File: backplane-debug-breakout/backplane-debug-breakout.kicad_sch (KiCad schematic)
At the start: 9 parts, among them J1 Conn_02x08_Odd_Even, J2 Conn_01x04, J3 Conn_01x01_Socket, J4 Conn_01x01_Socket, J5 Conn_01x04, SW1 SW_Push

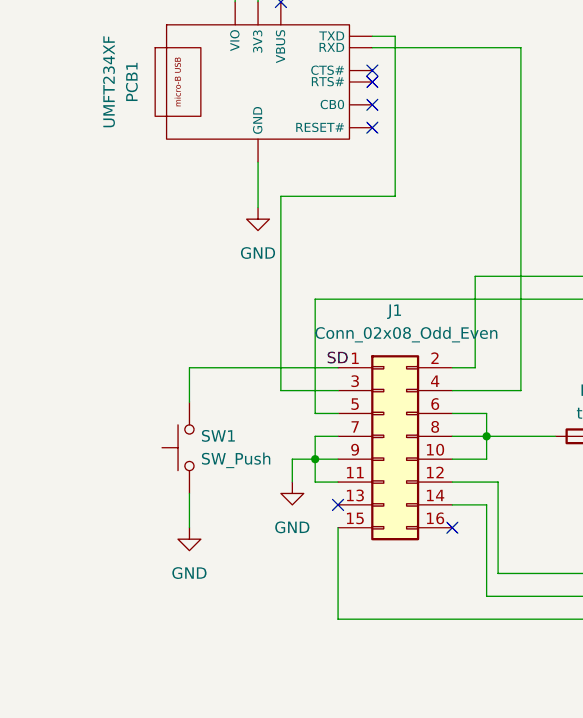
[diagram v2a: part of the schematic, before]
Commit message: added slide switch in parallel with push button
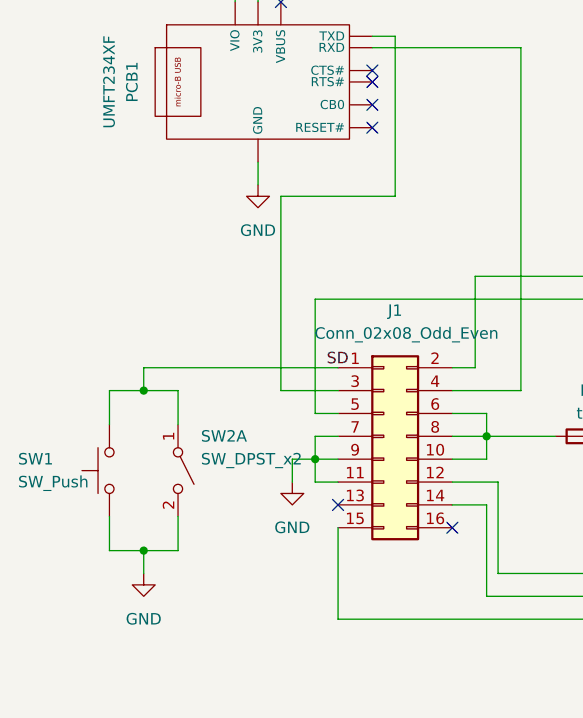
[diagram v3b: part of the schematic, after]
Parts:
- added SW2: SW_DPST_x2, symbol Switch:SW_DPST_x2
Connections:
- net GND: now also SW2.2 (B)
- net SD: now also SW2.1 (A)
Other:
- moved on the sheet: SW1
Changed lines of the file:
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@@
   (junction (at 101.6 82.55) (diameter 0) (color 0 0 0 0)
   )
+  (junction (at 82.55 74.93) (diameter 0) (color 0 0 0 0)
+  )
   (junction (at 120.65 80.01) (diameter 0) (color 0 0 0 0)
+  )
+  (junction (at 82.55 92.71) (diameter 0) (color 0 0 0 0)
   )
   (no_connect (at 148.59 67.31))
@@
     (stroke (width 0) (type default))
   )
+  (wire (pts (xy 78.74 74.93) (xy 82.55 74.93))
+    (stroke (width 0) (type default))
+  )
   (wire (pts (xy 101.6 82.55) (xy 101.6 85.09))
     (stroke (width 0) (type default))
   )
+  (wire (pts (xy 78.74 92.71) (xy 82.55 92.71))
+    (stroke (width 0) (type default))
+  )
   (wire (pts (xy 101.6 77.47) (xy 101.6 64.77))
     (stroke (width 0) (type default))
   )
+  (wire (pts (xy 78.74 78.74) (xy 78.74 74.93))
+    (stroke (width 0) (type default))
+  )
   (wire (pts (xy 116.84 82.55) (xy 120.65 82.55))
     (stroke (width 0) (type default))
@@
     (stroke (width 0) (type default))
   )
+  (wire (pts (xy 82.55 92.71) (xy 86.36 92.71))
+    (stroke (width 0) (type default))
+  )
   (wire (pts (xy 124.46 36.83) (xy 107.95 36.83))
     (stroke (width 0) (type default))
@@
     (stroke (width 0) (type default))
   )
-  (wire (pts (xy 87.63 72.39) (xy 104.14 72.39))
+  (wire (pts (xy 82.55 72.39) (xy 104.14 72.39))
     (stroke (width 0) (type default))
   )
@@
     (stroke (width 0) (type default))
   )
-  (wire (pts (xy 87.63 76.2) (xy 87.63 72.39))
-    (stroke (width 0) (type default))
-  )
   (wire (pts (xy 116.84 77.47) (xy 120.65 77.47))
     (stroke (width 0) (type default))
@@
     (stroke (width 0) (type default))
   )
-  (wire (pts (xy 87.63 86.36) (xy 87.63 90.17))
+  (wire (pts (xy 78.74 88.9) (xy 78.74 92.71))
     (stroke (width 0) (type default))
   )
@@
     (stroke (width 0) (type default))
   )
+  (wire (pts (xy 86.36 88.9) (xy 86.36 92.71))
+    (stroke (width 0) (type default))
+  )
+  (wire (pts (xy 82.55 92.71) (xy 82.55 95.25))
+    (stroke (width 0) (type default))
+  )
   (wire (pts (xy 101.6 80.01) (xy 101.6 82.55))
     (stroke (width 0) (type default))
@@
     (stroke (width 0) (type default))
   )
+  (wire (pts (xy 82.55 72.39) (xy 82.55 74.93))
+    (stroke (width 0) (type default))
+  )
   (wire (pts (xy 99.06 82.55) (xy 101.6 82.55))
     (stroke (width 0) (type default))
   )
+  (wire (pts (xy 86.36 74.93) (xy 86.36 78.74))
+    (stroke (width 0) (type default))
+  )
   (wire (pts (xy 154.94 83.82) (xy 154.94 86.36))
     (stroke (width 0) (type default))
   )
-  (wire (pts (xy 95.25 49.53) (xy 95.25 54.61))
+  (wire (pts (xy 82.55 74.93) (xy 86.36 74.93))
+    (stroke (width 0) (type default))
+  )
+  (wire (pts (xy 95.25 49.53) (xy 95.25 52.07))
     (stroke (width 0) (type default))
   )
@@
     )
   )
-  (symbol (lib_id "power:GND") (at 95.25 54.61 0) (unit 1)
+  (symbol (lib_id "power:GND") (at 95.25 52.07 0) (unit 1)
     (in_bom yes) (on_board yes) (dnp no) (fields_autoplaced)
-    (property "Reference" "#PWR06" (at 95.25 60.96 0)
-      (effects (font (size 1.27 1.27)) hide)
-    )
-    (property "Value" "GND" (at 95.25 59.69 0)
-      (effects (font (size 1.27 1.27)))
-    )
-    (property "Footprint" "" (at 95.25 54.61 0)
-      (effects (font (size 1.27 1.27)) hide)
-    )
-    (property "Datasheet" "" (at 95.25 54.61 0)
+    (property "Reference" "#PWR06" (at 95.25 58.42 0)
+      (effects (font (size 1.27 1.27)) hide)
+    )
+    (property "Value" "GND" (at 95.25 57.15 0)
+      (effects (font (size 1.27 1.27)))
+    )
+    (property "Footprint" "" (at 95.25 52.07 0)
+      (effects (font (size 1.27 1.27)) hide)
+    )
+    (property "Datasheet" "" (at 95.25 52.07 0)
       (effects (font (size 1.27 1.27)) hide)
     )
@@
     )
   )
-  (symbol (lib_id "power:GND") (at 87.63 90.17 0) (unit 1)
+  (symbol (lib_id "power:GND") (at 82.55 95.25 0) (unit 1)
     (in_bom yes) (on_board yes) (dnp no) (fields_autoplaced)
-    (property "Reference" "#PWR01" (at 87.63 96.52 0)
-      (effects (font (size 1.27 1.27)) hide)
-    )
-    (property "Value" "GND" (at 87.63 95.25 0)
-      (effects (font (size 1.27 1.27)))
-    )
-    (property "Footprint" "" (at 87.63 90.17 0)
-      (effects (font (size 1.27 1.27)) hide)
-    )
-    (property "Datasheet" "" (at 87.63 90.17 0)
+    (property "Reference" "#PWR01" (at 82.55 101.6 0)
+      (effects (font (size 1.27 1.27)) hide)
+    )
+    (property "Value" "GND" (at 82.55 100.33 0)
+      (effects (font (size 1.27 1.27)))
+    )
+    (property "Footprint" "" (at 82.55 95.25 0)
+      (effects (font (size 1.27 1.27)) hide)
+    )
+    (property "Datasheet" "" (at 82.55 95.25 0)
       (effects (font (size 1.27 1.27)) hide)
     )
@@
     )
   )
+  (symbol (lib_id "Switch:SW_DPST_x2") (at 86.36 83.82 270) (unit 1)
+    (in_bom yes) (on_board yes) (dnp no)
+    (property "Reference" "SW2" (at 88.9 80.01 90)
+      (effects (font (size 1.27 1.27)) (justify left))
+    )
+    (property "Value" "SW_DPST_x2" (at 88.9 82.55 90)
+      (effects (font (size 1.27 1.27)) (justify left))
+    )
+    (property "Footprint" "" (at 86.36 83.82 0)
+      (effects (font (size 1.27 1.27)) hide)
+    )
+    (property "Datasheet" "~" (at 86.36 83.82 0)
+      (effects (font (size 1.27 1.27)) hide)
+    )
+    (pin "4")
+    (pin "3")
+    (pin "2")
+    (pin "1")
+    (instances
+      (project "backplane-debug-breakout"
+        (path "/3c6f9748-3b52-445b-9cee-a3f7ec926272"
+          (reference "SW2") (unit 1)
+        )
+      )
+    )
+  )
   (symbol (lib_id "Connector_Generic:Conn_01x04") (at 153.67 62.23 0) (unit 1)
     (in_bom yes) (on_board yes) (dnp no)
@@
     )
   )
-  (symbol (lib_id "Switch:SW_Push") (at 87.63 81.28 90) (unit 1)
-    (in_bom yes) (on_board yes) (dnp no) (fields_autoplaced)
-    (property "Reference" "SW1" (at 88.9 80.01 90)
+  (symbol (lib_id "Switch:SW_Push") (at 78.74 83.82 90) (unit 1)
+    (in_bom yes) (on_board yes) (dnp no)
+    (property "Reference" "SW1" (at 68.58 82.55 90)
       (effects (font (size 1.27 1.27)) (justify right))
     )
-    (property "Value" "SW_Push" (at 88.9 82.55 90)
+    (property "Value" "SW_Push" (at 68.58 85.09 90)
       (effects (font (size 1.27 1.27)) (justify right))
     )
-    (property "Footprint" "" (at 82.55 81.28 0)
-      (effects (font (size 1.27 1.27)) hide)
-    )
-    (property "Datasheet" "~" (at 82.55 81.28 0)
-      (effects (font (size 1.27 1.27)) hide)
-    )
+    (property "Footprint" "" (at 73.66 83.82 0)
+      (effects (font (size 1.27 1.27)) hide)
+    )
+    (property "Datasheet" "~" (at 73.66 83.82 0)
+      (effects (font (size 1.27 1.27)) hide)
+    )

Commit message: finished schematic.
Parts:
- removed F1: tbd, symbol Device:Fuse
- added F2: Fuse_Small, oresat-passives:Littelfuse 155900DR, symbol Device:Fuse_Small
- D1: footprint Diode_THT:D_DO-41_SOD81_P10.16mm_Horizontal -> oresat-diodes:Diode TSM MURS315SH
- J1: footprint (none) -> Connector_PinHeader_2.54mm:PinHeader_2x08_P2.54mm_Vertical
- J2: footprint (none) -> Connector_PinHeader_2.54mm:PinHeader_1x04_P2.54mm_Vertical
- J3, J4: footprint (none) -> Connector:Banana_Jack_1Pin
- J5: footprint (none) -> oresat-pcbs:vulCAN
- PCB1: footprint (none) -> oresat-misc:UMFT234XF
- SW1: footprint (none) -> Button_Switch_THT:SW_PUSH_1P1T_6x3.5mm_H4.3_APEM_MJTP1243
- SW2: footprint (none) -> Button_Switch_SMD:SW_DIP_SPSTx01_Slide_9.78x4.72mm_W8.61mm_P2.54mm
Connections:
- net at D1.1 (K): now also F2.2
- net at J1.10 (Pin_10), J1.6 (Pin_6), J1.8 (Pin_8): now also F2.1
- net C3-UART-TX: now reaches J1.3 (Pin_3), PCB1.P7 (TXD)
- net C3-UART-RX: now reaches J1.4 (Pin_4), PCB1.P9 (RXD)
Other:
- note added: "check switch footprints"
- moved on the sheet: SW1, SW2A

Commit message: updated schemcatic footprints
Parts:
- J1: footprint Connector_PinHeader_2.54mm:PinHeader_2x08_P2.54mm_Vertical -> Connector_IDC:IDC-Header_2x08_P2.54mm_Vertical
- J5: footprint oresat-pcbs:vulCAN -> Connector_PinHeader_2.54mm:PinHeader_1x04_P2.54mm_Vertical
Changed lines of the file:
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@@
 			)
 		)
-		(property "Datasheet" "http://www.vishay.com/docs/88503/1n4001.pdf"
+		(property "Datasheet" "https://services.taiwansemi.com/storage/resources/datasheet/MUR305SH%20SERIES_B2212.pdf"
 			(at 144.78 80.01 0)
 			(effects
@@
 			)
 		)
-		(property "Footprint" "Connector_PinHeader_2.54mm:PinHeader_2x08_P2.54mm_Vertical"
+		(property "Footprint" "Connector_IDC:IDC-Header_2x08_P2.54mm_Vertical"
 			(at 109.22 80.01 0)
 			(effects
@@
 			)
 		)
-		(property "Footprint" "oresat-pcbs:vulCAN"
+		(property "Footprint" "Connector_PinHeader_2.54mm:PinHeader_1x04_P2.54mm_Vertical"
 			(at 153.67 62.23 0)
 			(effects

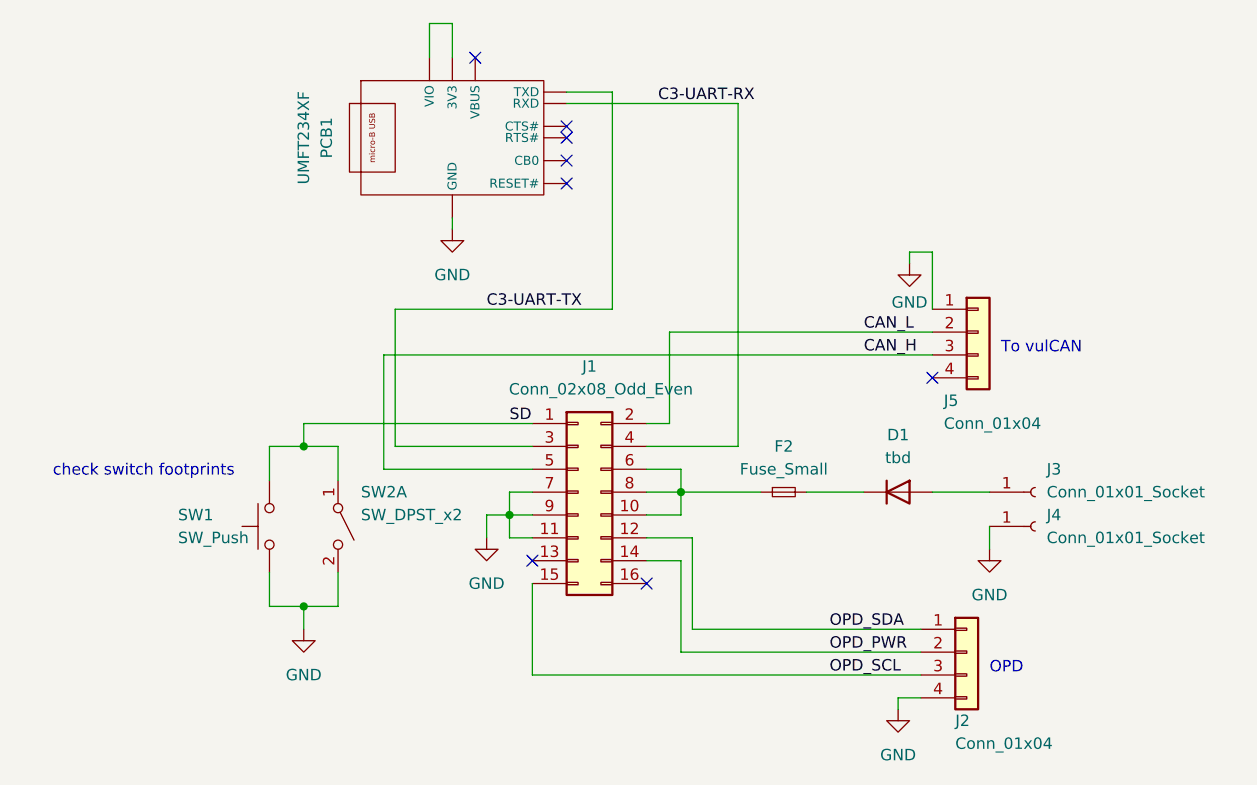
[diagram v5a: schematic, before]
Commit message: added part numbers to schematic
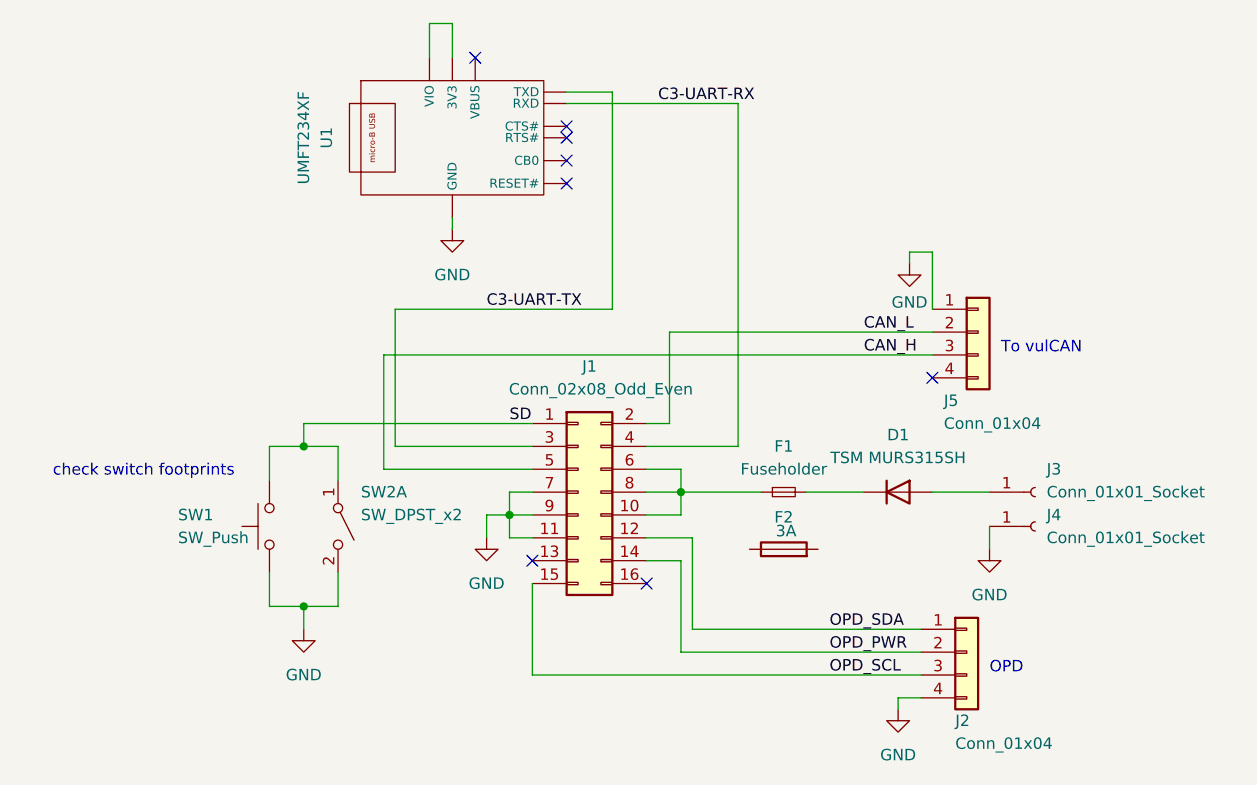
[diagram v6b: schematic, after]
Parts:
- added F2: 3A, symbol Device:Fuse
- D1: value tbd -> TSM MURS315SH; DPN (none) -> 1801-MUR315SHCT-ND; MPN (none) -> MUR315SH
- F1: renamed from F2; value Fuse_Small -> Fuseholder; DPN (none) -> 18-01550900DRCT-ND; MPN (none) -> 01550900DR
- J1: DPN (none) -> 609-86130161014345E1LF-ND; MPN (none) -> 86130161014345E1LF
- J2, J5: DPN (none) -> WM12840-ND; MPN (none) -> 0757570441
- J3, J4: now left out of the parts list
- U1: renamed from PCB1; DPN (none) -> 768-1174-ND; MPN (none) -> UMFT234XF

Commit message: added switches
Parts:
- SW1: footprint Button_Switch_THT:SW_PUSH_1P1T_6x3.5mm_H4.3_APEM_MJTP1243 -> oresat-misc:D6R90_CNK
- SW2: footprint Button_Switch_SMD:SW_DIP_SPSTx01_Slide_9.78x4.72mm_W8.61mm_P2.54mm -> Connector_PinHeader_2.54mm:PinHeader_1x03_P2.54mm_Vertical; DPN (none) -> EG1903-ND; MPN (none) -> EG1218
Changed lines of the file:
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@@
 			)
 		)
-		(property "Footprint" "Button_Switch_SMD:SW_DIP_SPSTx01_Slide_9.78x4.72mm_W8.61mm_P2.54mm"
+		(property "Footprint" "Connector_PinHeader_2.54mm:PinHeader_1x03_P2.54mm_Vertical"
 			(at 82.55 83.82 0)
 			(effects
@@
 			)
 		)
-		(property "DPN" ""
-			(at 82.55 83.82 0)
-			(effects
-				(font
-					(size 1.27 1.27)
-				)
-				(hide yes)
-			)
-		)
-		(property "MPN" ""
+		(property "DPN" "EG1903-ND"
+			(at 82.55 83.82 0)
+			(effects
+				(font
+					(size 1.27 1.27)
+				)
+				(hide yes)
+			)
+		)
+		(property "MPN" "EG1218"
 			(at 82.55 83.82 0)
 			(effects
@@
 			)
 		)
-		(property "Footprint" "Button_Switch_THT:SW_PUSH_1P1T_6x3.5mm_H4.3_APEM_MJTP1243"
+		(property "Footprint" "oresat-misc:D6R90_CNK"
 			(at 69.85 83.82 0)
 			(effects
@@
 			)
 		)
-		(property "Datasheet" "~"
+		(property "Datasheet" "https://www.ckswitches.com/media/1341/d6.pdf"
 			(at 69.85 83.82 0)
 			(effects

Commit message: added part numbers to BOM
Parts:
- SW1: DPN (none) -> 401-1995-ND; MPN (none) -> D6R90 F2 LFS
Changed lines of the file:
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@@
 			)
 		)
-		(property "Datasheet" "~"
+		(property "Datasheet" "https://sten-eswitch-13110800-production.s3.amazonaws.com/system/asset/product_line/data_sheet/119/EG.pdf"
 			(at 82.55 83.82 0)
 			(effects
@@
 			)
 		)
-		(property "DPN" ""
+		(property "DPN" "401-1995-ND"
 			(at 74.93 83.82 0)
 			(effects
@@
 			)
 		)
-		(property "MPN" ""
+		(property "MPN" "D6R90 F2 LFS"
 			(at 74.93 83.82 0)
 			(effects
